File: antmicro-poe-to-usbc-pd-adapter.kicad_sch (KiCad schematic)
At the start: 0 parts

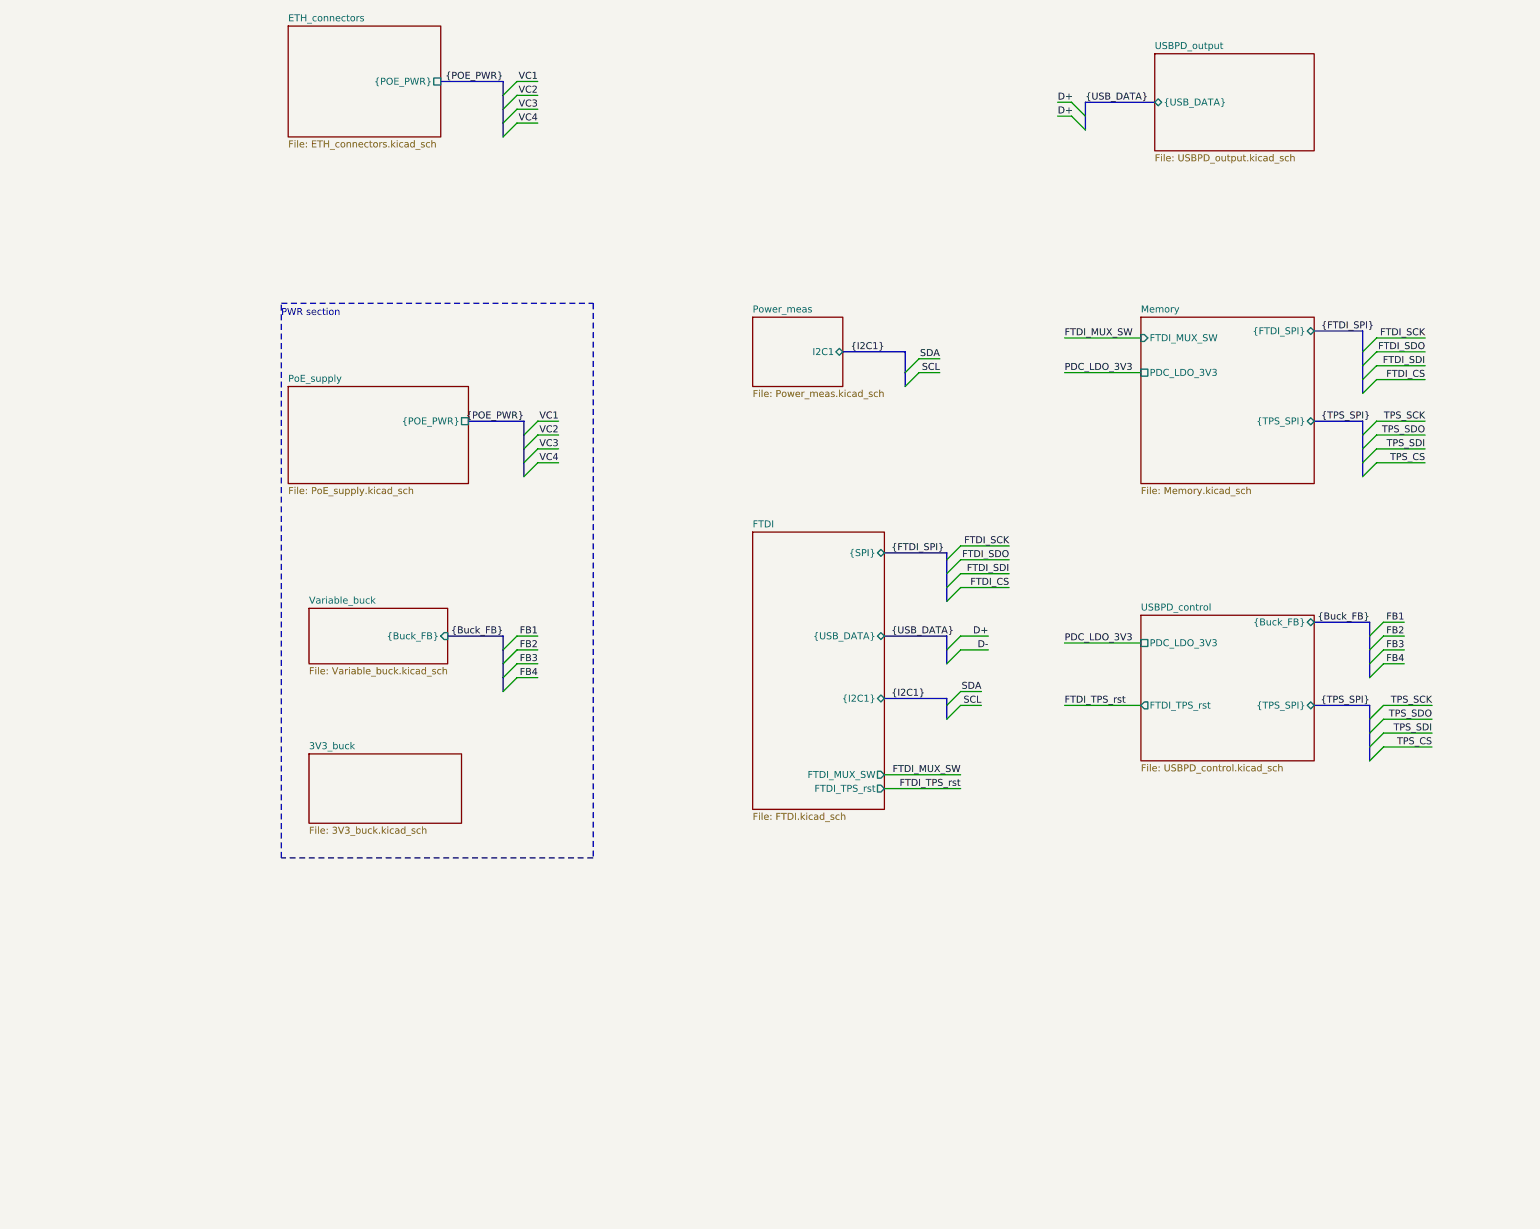
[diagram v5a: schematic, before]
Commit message: [#62623] Improve schematic, change 3V3 buck inductor, correct SPI, add testpoint
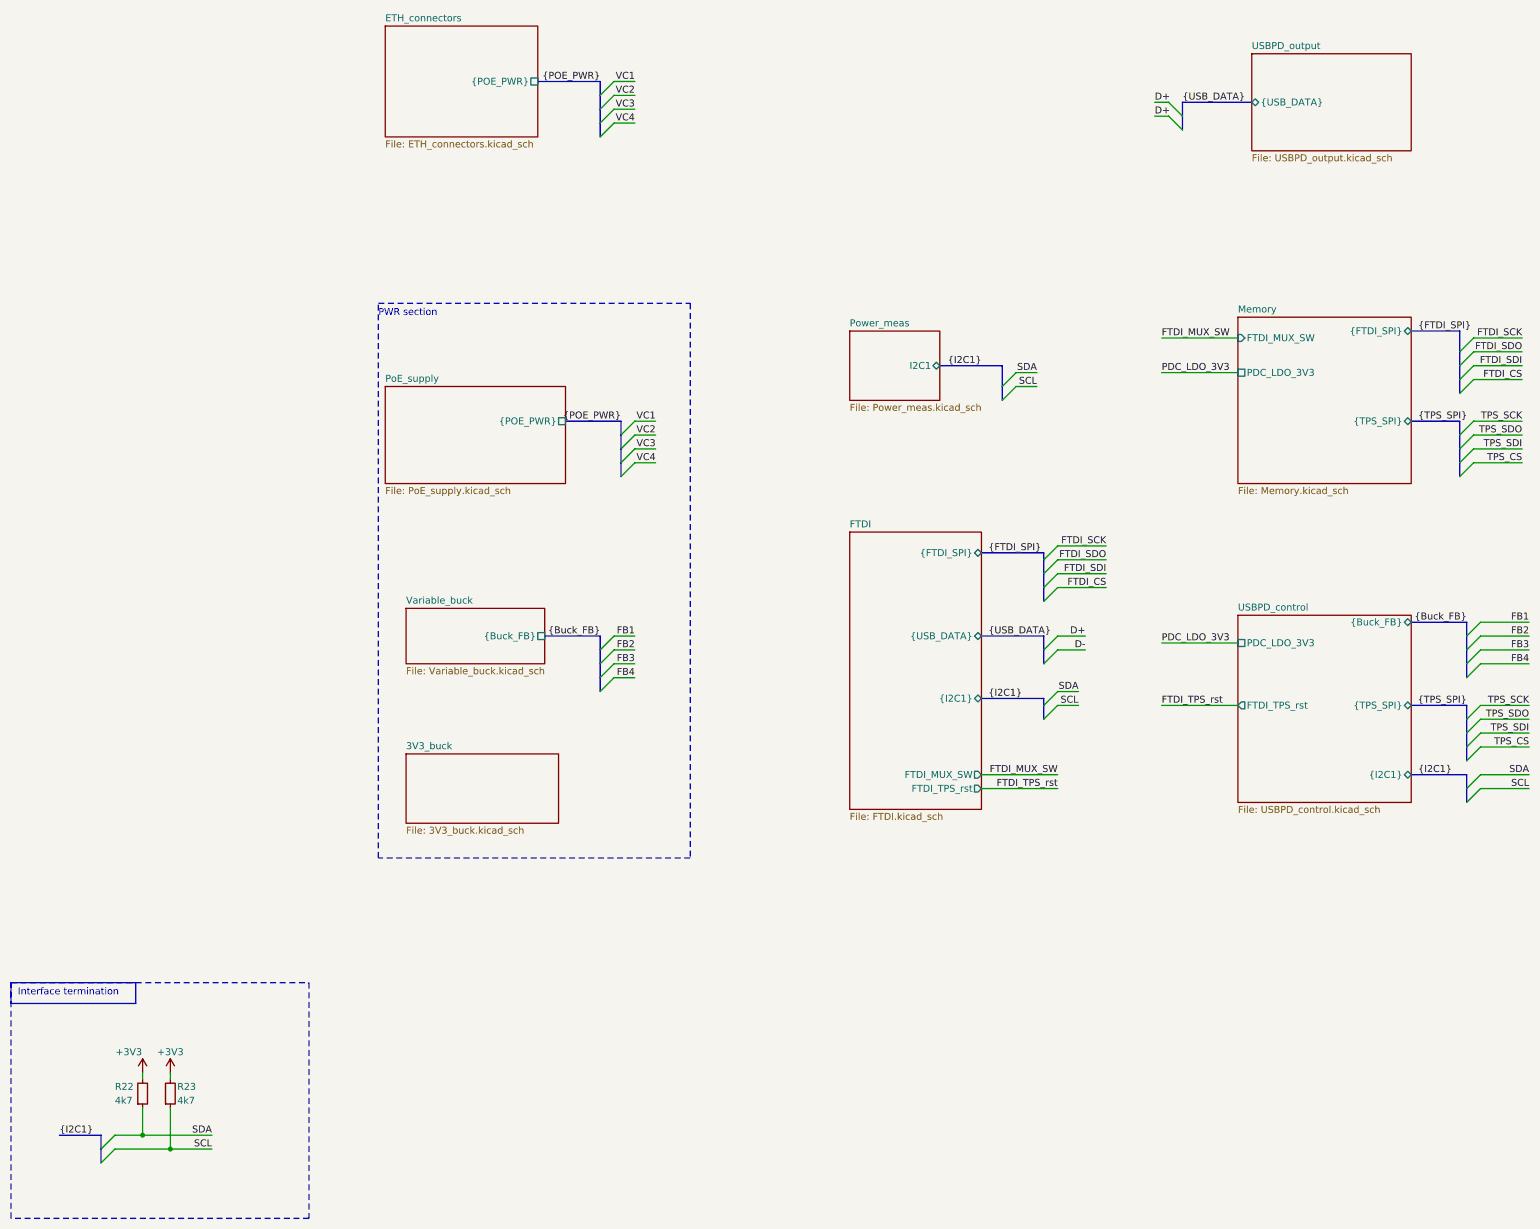
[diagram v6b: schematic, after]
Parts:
- added R22, R23: R_4k7_0402, antmicro-footprints:R_0402_1005Metric, symbol antmicroResistors0402:R_4k7_0402
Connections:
- net SCL: now also R23.1
- net SDA: now also R22.1
- new net +3V3: R22.2, R23.2
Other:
- sheet FTDI ports: added {FTDI_SPI}; removed {SPI}
- sheet USBPD_control ports: added {I2C1}; removed none
- note added: "Interface termination"

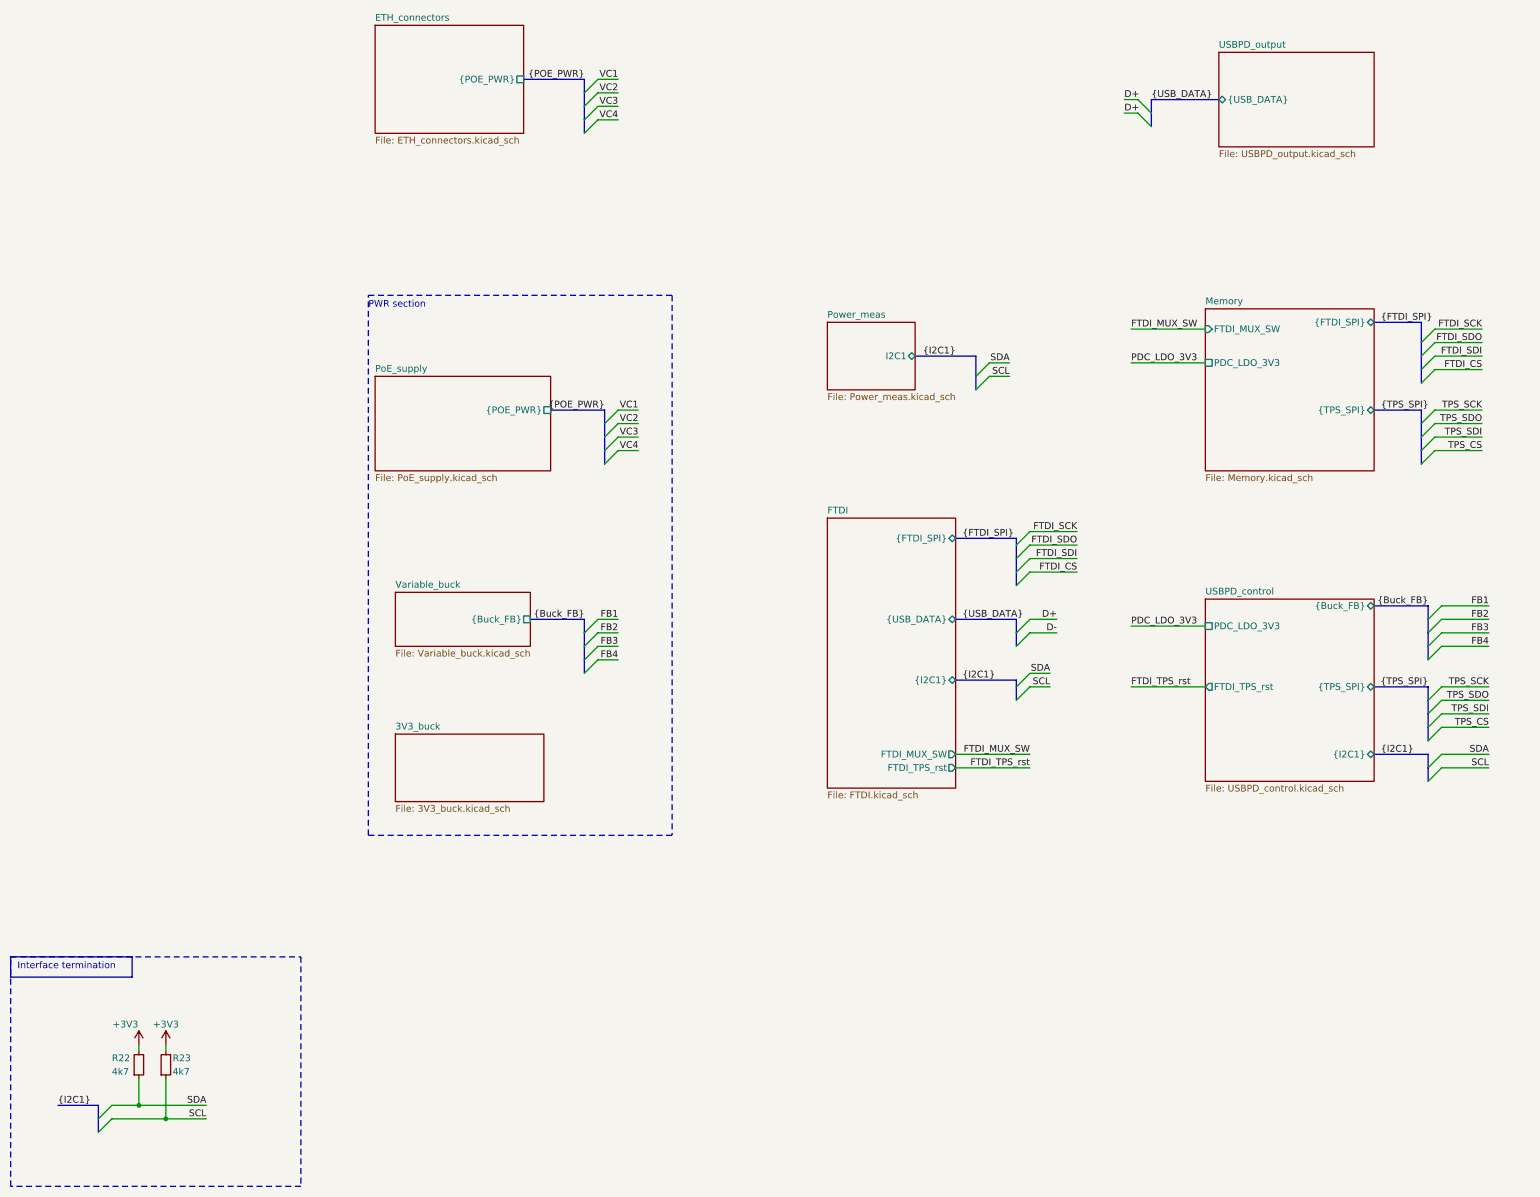
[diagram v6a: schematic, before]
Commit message: [#62623] Change hierarchy implementation
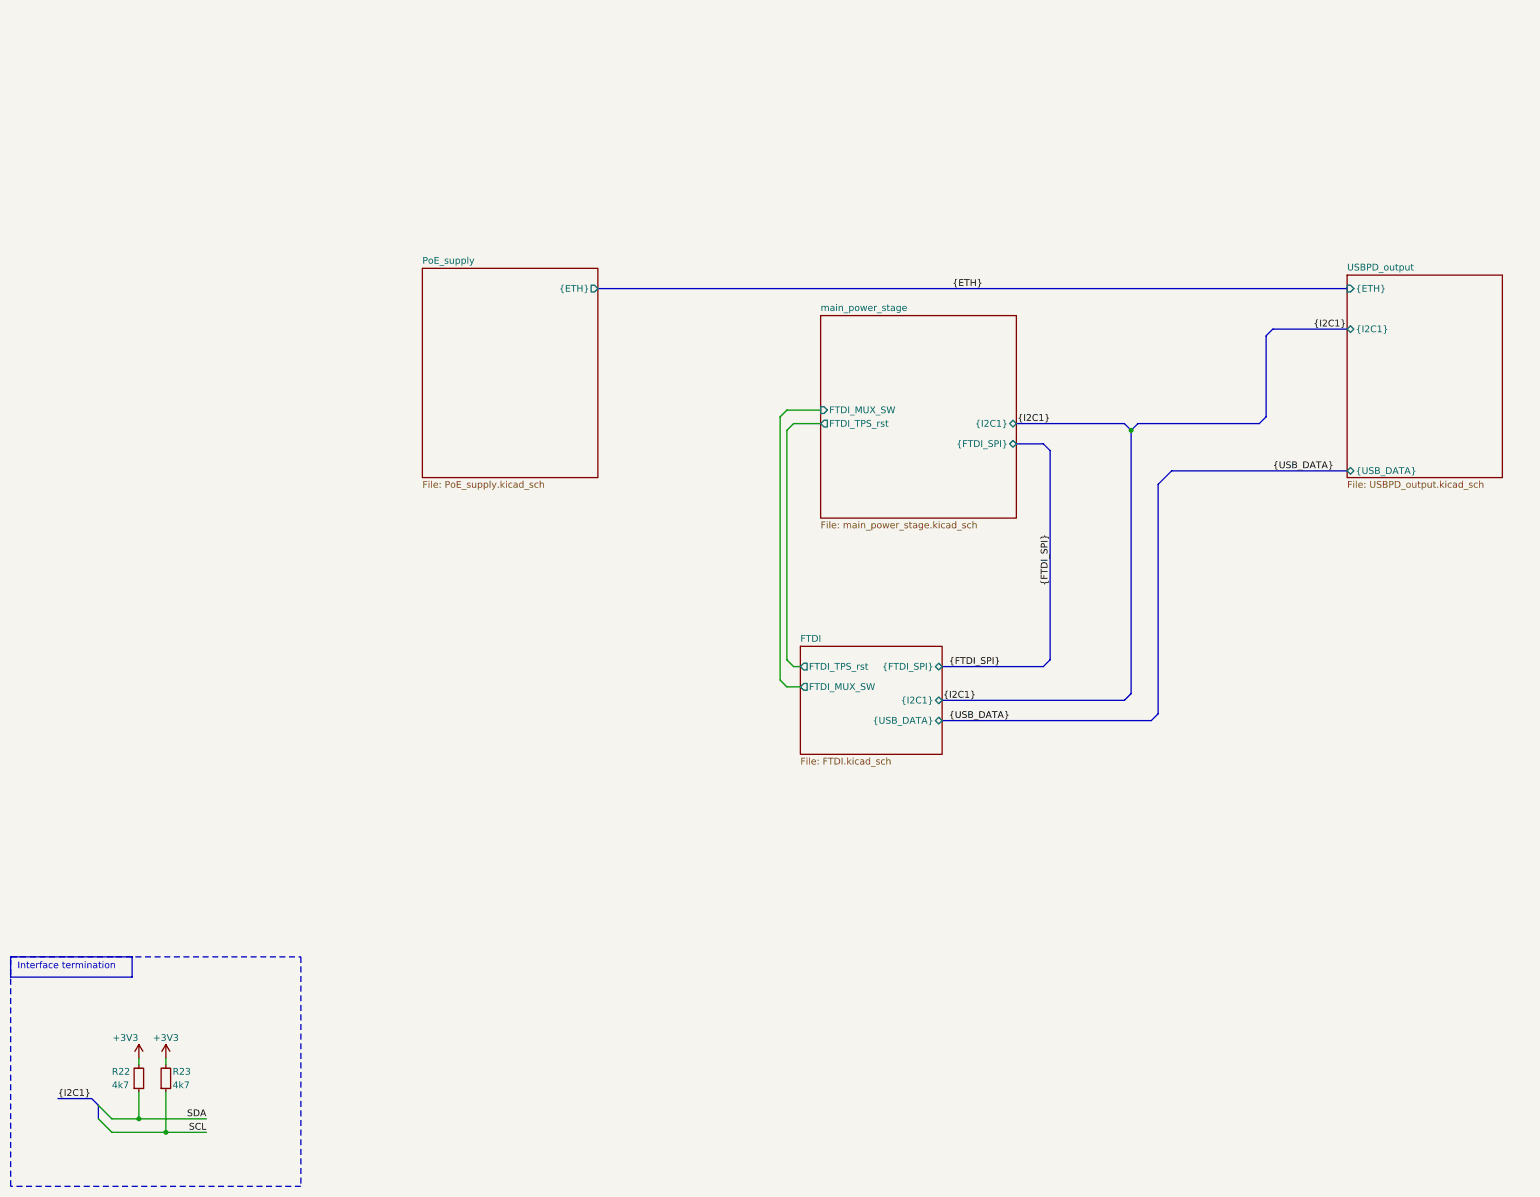
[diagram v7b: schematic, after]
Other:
- removed sheet 3V3_buck
- removed sheet ETH_connectors
- removed sheet Memory
- removed sheet Power_meas
- removed sheet USBPD_control
- removed sheet Variable_buck
- added sheet main_power_stage (main_power_stage.kicad_sch)
- sheet PoE_supply ports: added {ETH}; removed {POE_PWR}
- sheet USBPD_output ports: added {ETH}, {I2C1}; removed none
- note removed: "PWR section"
- moved on the sheet: R22, R23

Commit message: [#62623] Minor graphical changes
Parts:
- removed R22, R23: R_4k7_0402, antmicro-footprints:R_0402_1005Metric, symbol antmicroResistors0402:R_4k7_0402
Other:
- note removed: "Interface termination"
